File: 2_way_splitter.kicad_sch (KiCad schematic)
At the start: 4 parts

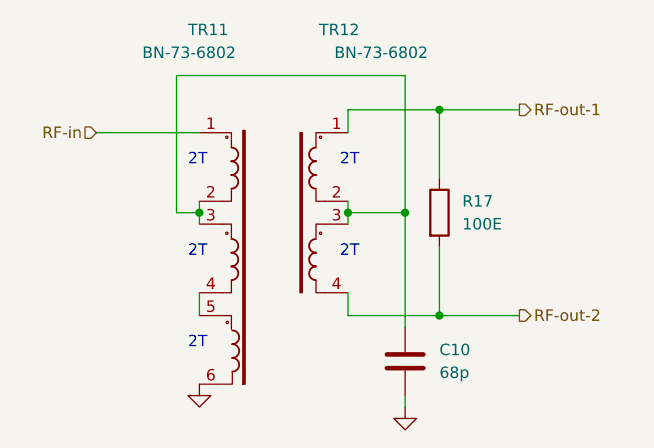
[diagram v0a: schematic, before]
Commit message: changed to 1 to 6
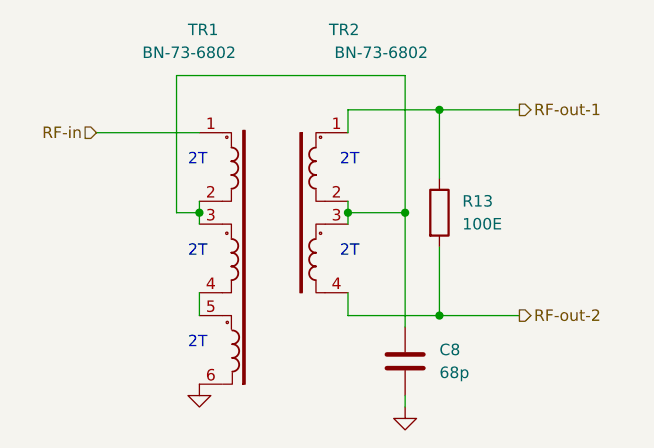
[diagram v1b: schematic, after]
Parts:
- removed C10: 68p, Capacitor_THT:C_Disc_D5.1mm_W3.2mm_P5.00mm, symbol Device:C
- added C8: 68p, Capacitor_SMD:C_0805_2012Metric_Pad1.18x1.45mm_HandSolder, symbol Device:C
- R13: renamed from R17; footprint Resistor_THT:R_Axial_DIN0411_L9.9mm_D3.6mm_P12.70mm_Horizontal -> Resistor_SMD:R_1206_3216Metric_Pad1.30x1.75mm_HandSolder
- renumbered TR11 to TR1, TR12 to TR2
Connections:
- net GND: now also C8.2
- net at TR1.2, TR1.3, TR2.2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: now also C8.1
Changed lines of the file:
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@@
     (effects (font (size 1.27 1.27)) (justify right))
-  )
-  (symbol (lib_id "Device:C") (at 133.35 104.14 0) (unit 1)
-    (in_bom yes) (on_board yes) (fields_autoplaced)
-    (property "Reference" "C10" (id 0) (at 137.16 102.8699 0)
-      (effects (font (size 1.27 1.27)) (justify left))
-    )
-    (property "Value" "68p" (id 1) (at 137.16 105.4099 0)
-      (effects (font (size 1.27 1.27)) (justify left))
-    )
-    (property "Footprint" "Capacitor_THT:C_Disc_D5.1mm_W3.2mm_P5.00mm" (id 2) (at 134.3152 107.95 0)
-      (effects (font (size 1.27 1.27)) hide)
-    )
-    (property "Datasheet" "~" (id 3) (at 133.35 104.14 0)
-      (effects (font (size 1.27 1.27)) hide)
-    )
-    (pin "1")
-    (pin "2")
   )
   (symbol (lib_id "power:GND") (at 133.35 109.22 0) (mirror y) (unit 1)
     (in_bom yes) (on_board yes) (fields_autoplaced)
-    (property "Reference" "#PWR049" (id 0) (at 133.35 115.57 0)
+    (property "Reference" "#PWR042" (id 0) (at 133.35 115.57 0)
       (effects (font (size 1.27 1.27)) hide)
     )
@@
   (symbol (lib_id "Components:BN-73-bifilar") (at 127 78.74 0) (mirror y) (unit 1)
     (in_bom yes) (on_board yes)
-    (property "Reference" "TR12" (id 0) (at 128.27 67.31 0)
+    (property "Reference" "TR2" (id 0) (at 128.27 67.31 0)
       (effects (font (size 1.27 1.27)) (justify left))
     )
@@
   (symbol (lib_id "Device:R") (at 137.16 87.63 0) (unit 1)
     (in_bom yes) (on_board yes) (fields_autoplaced)
-    (property "Reference" "R17" (id 0) (at 139.7 86.3599 0)
+    (property "Reference" "R13" (id 0) (at 139.7 86.3599 0)
       (effects (font (size 1.27 1.27)) (justify left))
     )
@@
       (effects (font (size 1.27 1.27)) (justify left))
     )
-    (property "Footprint" "Resistor_THT:R_Axial_DIN0411_L9.9mm_D3.6mm_P12.70mm_Horizontal" (id 2) (at 135.382 87.63 90)
+    (property "Footprint" "Resistor_SMD:R_1206_3216Metric_Pad1.30x1.75mm_HandSolder" (id 2) (at 135.382 87.63 90)
       (effects (font (size 1.27 1.27)) hide)
     )
@@
   (symbol (lib_id "Components:BN-73-trifilar") (at 110.49 78.74 0) (unit 1)
     (in_bom yes) (on_board yes)
-    (property "Reference" "TR11" (id 0) (at 109.22 67.31 0)
+    (property "Reference" "TR1" (id 0) (at 109.22 67.31 0)
       (effects (font (size 1.27 1.27)) (justify left))
     )
@@
     (pin "6")
   )
+  (symbol (lib_id "Device:C") (at 133.35 104.14 0) (unit 1)
+    (in_bom yes) (on_board yes) (fields_autoplaced)
+    (property "Reference" "C8" (id 0) (at 137.16 102.8699 0)
+      (effects (font (size 1.27 1.27)) (justify left))
+    )
+    (property "Value" "68p" (id 1) (at 137.16 105.4099 0)
+      (effects (font (size 1.27 1.27)) (justify left))
+    )
+    (property "Footprint" "Capacitor_SMD:C_0805_2012Metric_Pad1.18x1.45mm_HandSolder" (id 2) (at 134.3152 107.95 0)
+      (effects (font (size 1.27 1.27)) hide)
+    )
+    (property "Datasheet" "~" (id 3) (at 133.35 104.14 0)
+      (effects (font (size 1.27 1.27)) hide)
+    )
+    (pin "1")
+    (pin "2")
+  )
   (symbol (lib_id "power:GND") (at 110.49 106.68 0) (unit 1)
     (in_bom yes) (on_board yes) (fields_autoplaced)
-    (property "Reference" "#PWR048" (id 0) (at 110.49 113.03 0)
+    (property "Reference" "#PWR041" (id 0) (at 110.49 113.03 0)
       (effects (font (size 1.27 1.27)) hide)
     )

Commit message: pcb routed and made gerbers
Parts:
- renumbered C8 to C7
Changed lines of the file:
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@@
   (symbol (lib_id "Device:C") (at 133.35 104.14 0) (unit 1)
     (in_bom yes) (on_board yes) (fields_autoplaced)
-    (property "Reference" "C8" (id 0) (at 137.16 102.8699 0)
+    (property "Reference" "C7" (id 0) (at 137.16 102.8699 0)
       (effects (font (size 1.27 1.27)) (justify left))
     )

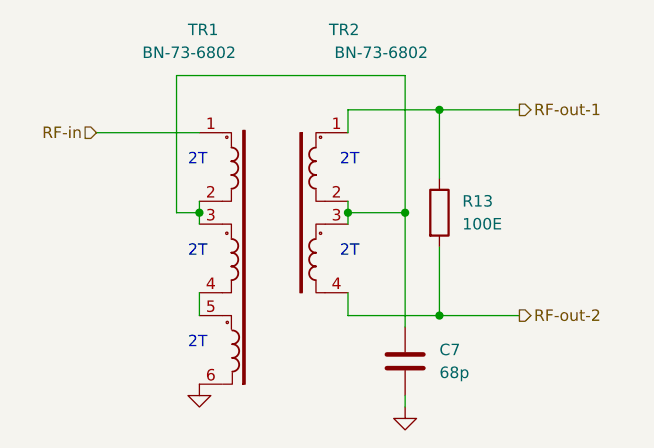
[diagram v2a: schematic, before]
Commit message: changed footprint for 2-way splitter transformer
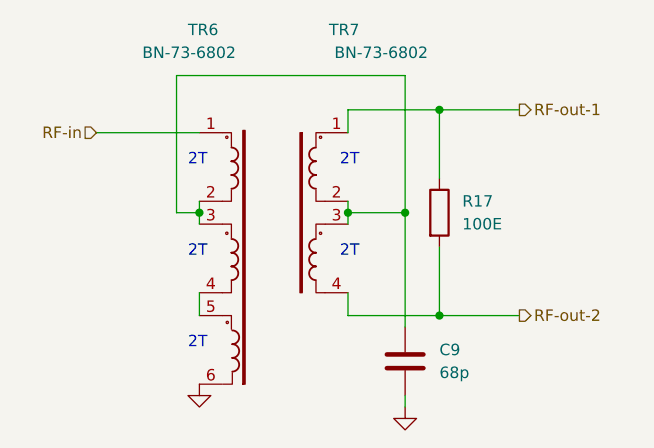
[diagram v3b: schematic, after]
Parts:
- TR7: renamed from TR2; footprint Components:BN-73-202-2-0 -> Components:BN-73-6802-2-0
- renumbered C7 to C9, R13 to R17, TR1 to TR6
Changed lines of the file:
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@@
   (symbol (lib_id "power:GND") (at 133.35 109.22 0) (mirror y) (unit 1)
     (in_bom yes) (on_board yes) (fields_autoplaced)
-    (property "Reference" "#PWR042" (id 0) (at 133.35 115.57 0)
+    (property "Reference" "#PWR0134" (id 0) (at 133.35 115.57 0)
       (effects (font (size 1.27 1.27)) hide)
     )
@@
   (symbol (lib_id "Components:BN-73-bifilar") (at 127 78.74 0) (mirror y) (unit 1)
     (in_bom yes) (on_board yes)
-    (property "Reference" "TR2" (id 0) (at 128.27 67.31 0)
+    (property "Reference" "TR7" (id 0) (at 128.27 67.31 0)
       (effects (font (size 1.27 1.27)) (justify left))
     )
@@
       (effects (font (size 1.27 1.27)) (justify left))
     )
-    (property "Footprint" "Components:BN-73-202-2-0" (id 2) (at 124.46 99.06 0)
+    (property "Footprint" "Components:BN-73-6802-2-0" (id 2) (at 124.46 99.06 0)
       (effects (font (size 1.27 1.27) italic) hide)
     )
@@
   (symbol (lib_id "Device:R") (at 137.16 87.63 0) (unit 1)
     (in_bom yes) (on_board yes) (fields_autoplaced)
-    (property "Reference" "R13" (id 0) (at 139.7 86.3599 0)
+    (property "Reference" "R17" (id 0) (at 139.7 86.3599 0)
       (effects (font (size 1.27 1.27)) (justify left))
     )
@@
   (symbol (lib_id "Components:BN-73-trifilar") (at 110.49 78.74 0) (unit 1)
     (in_bom yes) (on_board yes)
-    (property "Reference" "TR1" (id 0) (at 109.22 67.31 0)
+    (property "Reference" "TR6" (id 0) (at 109.22 67.31 0)
       (effects (font (size 1.27 1.27)) (justify left))
     )
@@
   (symbol (lib_id "Device:C") (at 133.35 104.14 0) (unit 1)
     (in_bom yes) (on_board yes) (fields_autoplaced)
-    (property "Reference" "C7" (id 0) (at 137.16 102.8699 0)
+    (property "Reference" "C9" (id 0) (at 137.16 102.8699 0)
       (effects (font (size 1.27 1.27)) (justify left))
     )
@@
   (symbol (lib_id "power:GND") (at 110.49 106.68 0) (unit 1)
     (in_bom yes) (on_board yes) (fields_autoplaced)
-    (property "Reference" "#PWR041" (id 0) (at 110.49 113.03 0)
+    (property "Reference" "#PWR0135" (id 0) (at 110.49 113.03 0)
       (effects (font (size 1.27 1.27)) hide)
     )
